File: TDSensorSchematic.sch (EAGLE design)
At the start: 11 parts, among them U1 MPL3115A2LGA8, U2 ADXL345PATRICK

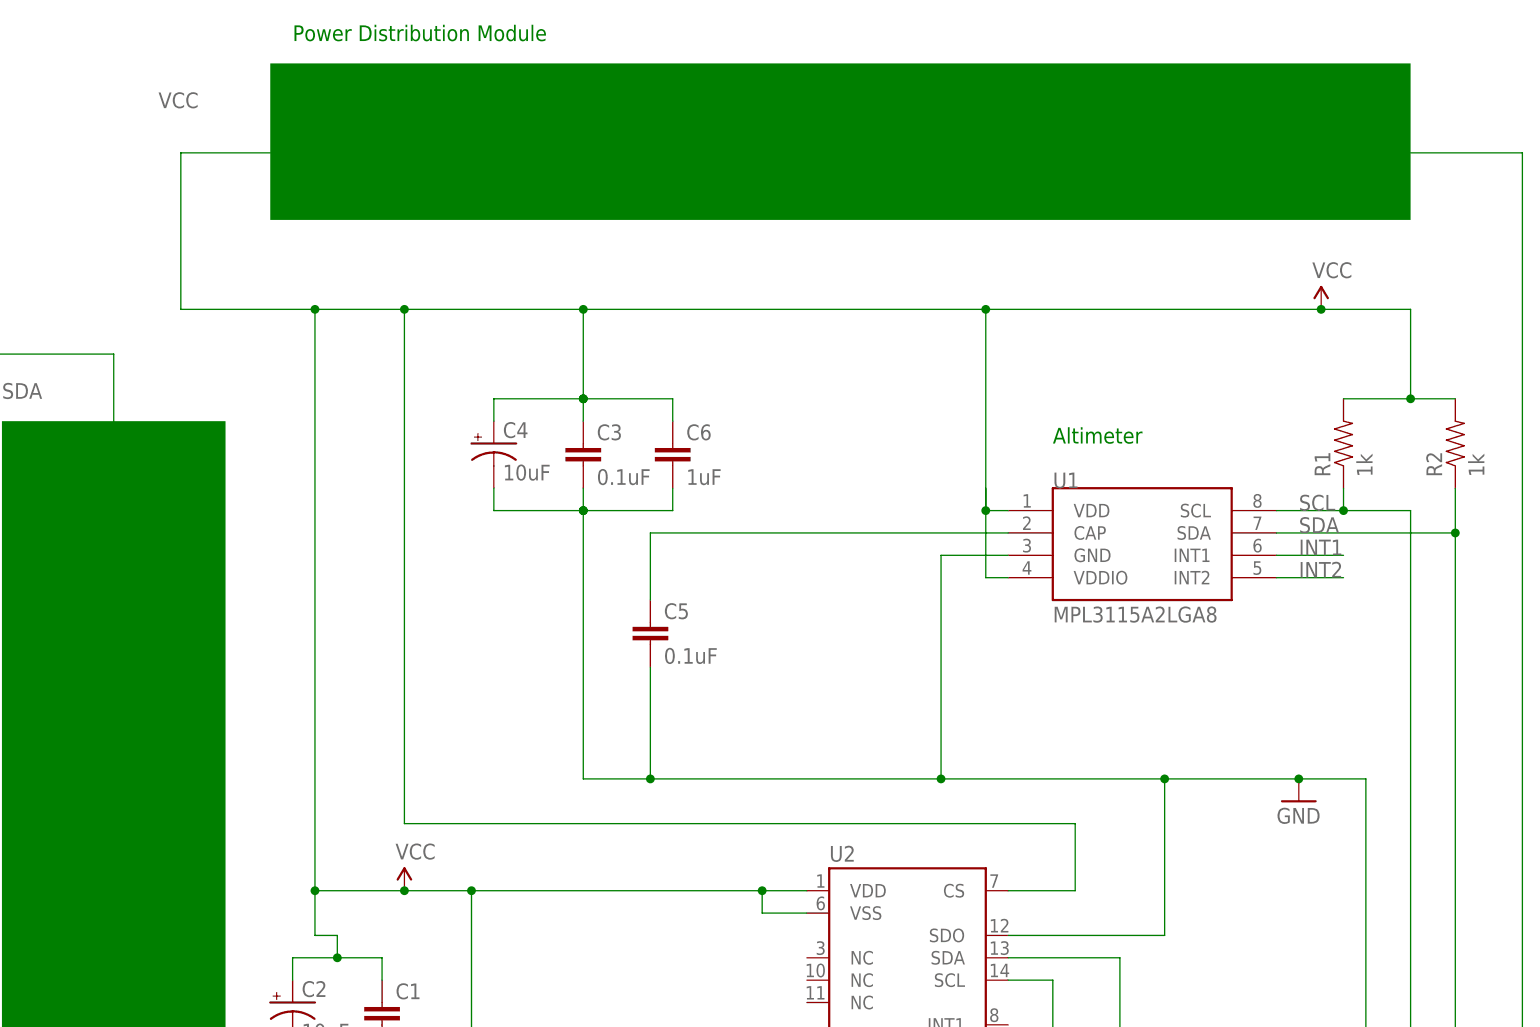
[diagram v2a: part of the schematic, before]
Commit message: labeled VCC 3.3V
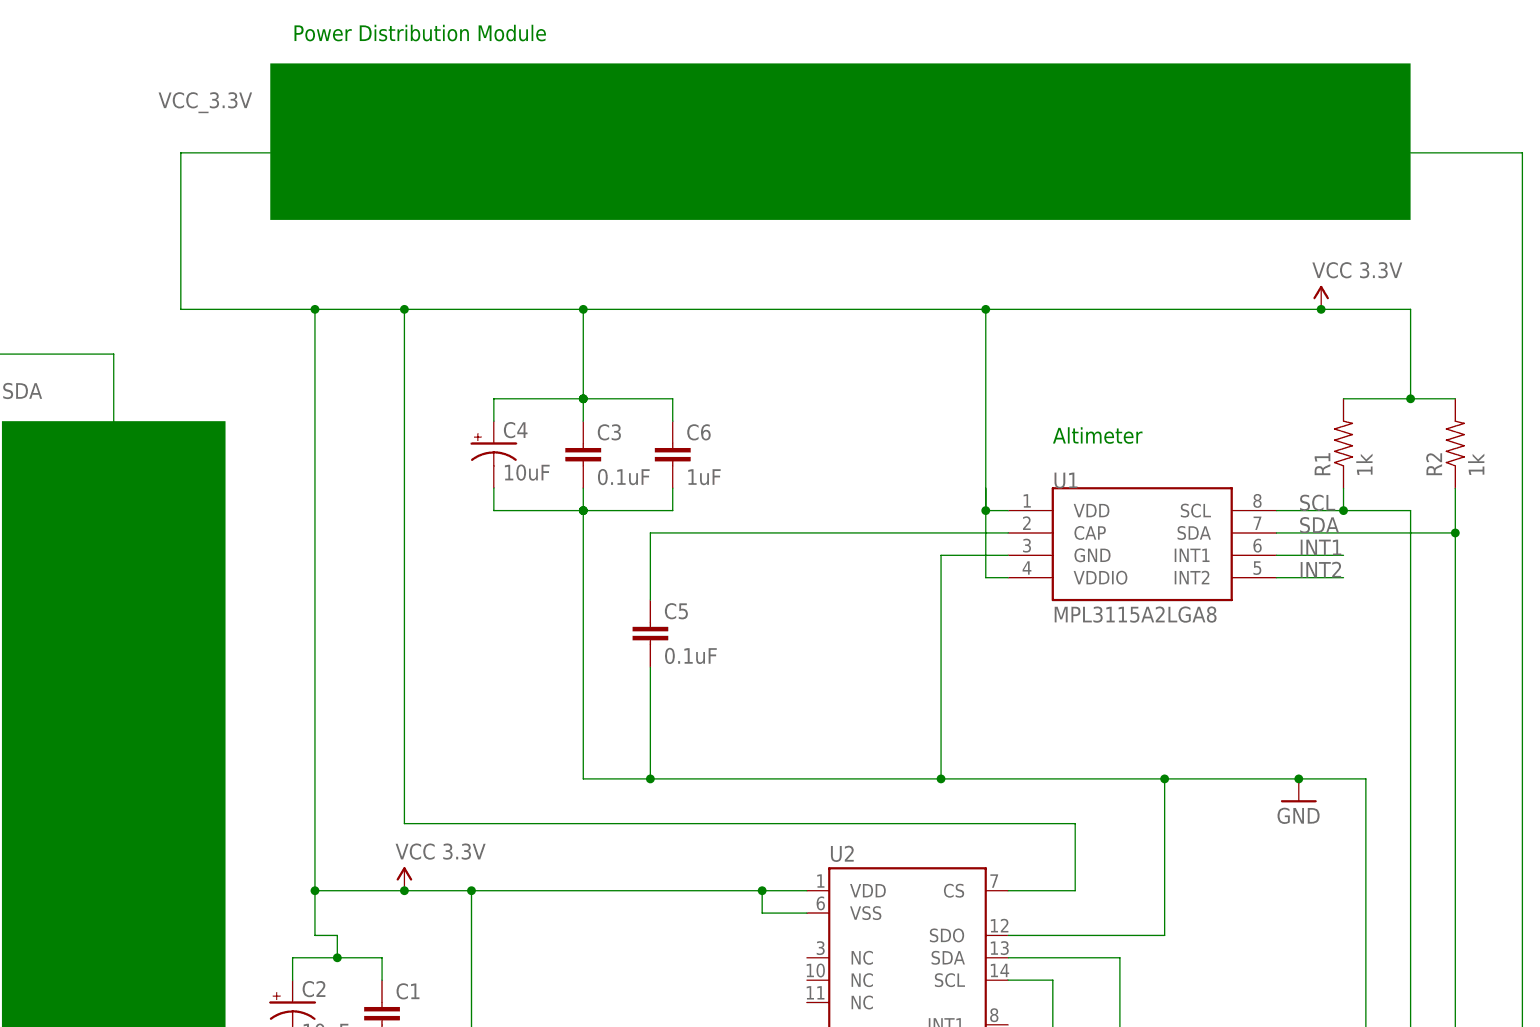
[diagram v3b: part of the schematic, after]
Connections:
- net VCC renamed VCC_3.3V
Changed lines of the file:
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@@
 <parts>
 <part name="C1" library="SparkFun" deviceset="CAP" device="0603-CAP" value="0.1uF"/>
-<part name="P+2" library="SparkFun" deviceset="VCC" device=""/>
+<part name="P+2" library="SparkFun" deviceset="VCC" device="" value="VCC 3.3V"/>
 <part name="CIO" library="SparkFun" deviceset="CAP" device="0603-CAP" value="0.1uF"/>
 <part name="GND4" library="SparkFun" deviceset="GND" device=""/>
@@
 <part name="GND5" library="SparkFun" deviceset="GND" device=""/>
 <part name="C6" library="SparkFun" deviceset="CAP" device="0402-CAP" value="1uF"/>
-<part name="P+1" library="SparkFun" deviceset="VCC" device=""/>
+<part name="P+1" library="SparkFun" deviceset="VCC" device="" value="VCC 3.3V"/>
 </parts>
 <sheets>
@@
 </segment>
 </net>
-<net name="VCC" class="0">
+<net name="VCC_3.3V" class="0">
 <segment>
 <wire x1="83.82" y1="114.3" x2="81.28" y2="114.3" width="0.1524" layer="91"/>
